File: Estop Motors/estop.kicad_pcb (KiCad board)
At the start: 2 copper layers, 28 parts, among them Q1 IRF9530N, Q2 IRF9530N, Q3 IRF9530N, Q4 IRF9530N

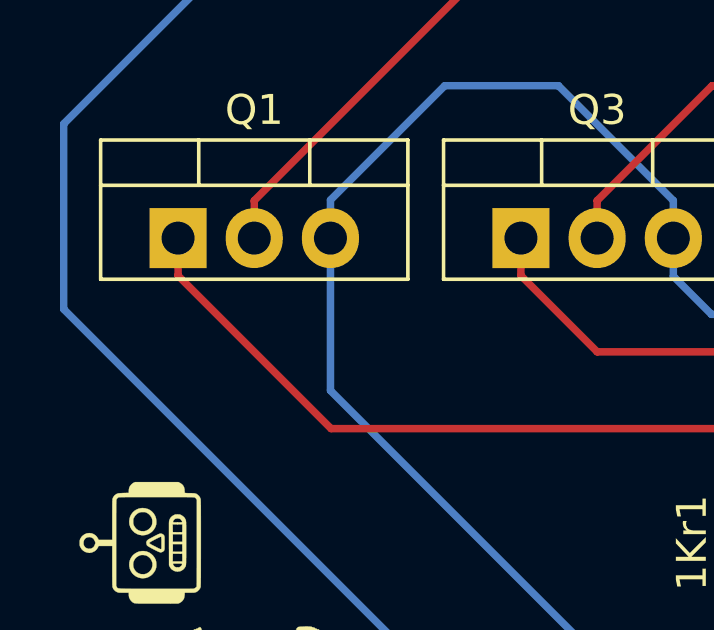
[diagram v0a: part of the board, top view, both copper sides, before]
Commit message: Fixed Silkscreen
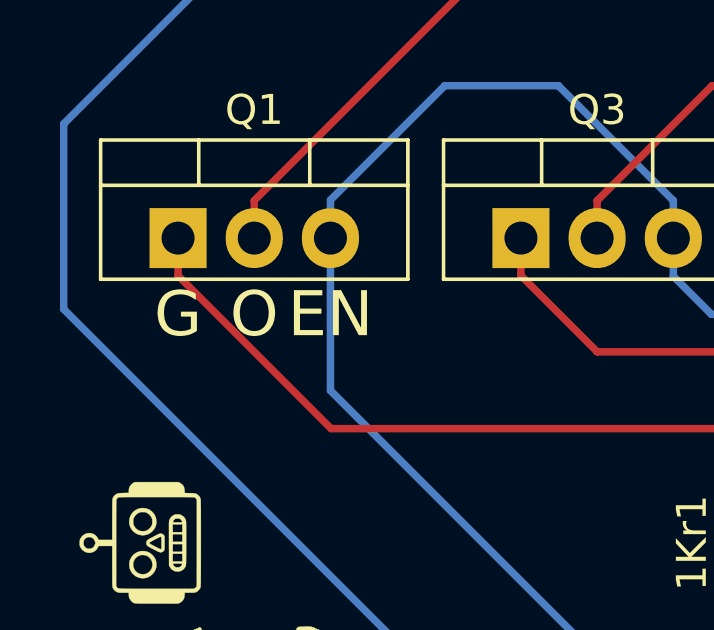
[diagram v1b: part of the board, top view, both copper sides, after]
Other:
- board text added: "EN"
- board text added: "G"
- board text added: "O"
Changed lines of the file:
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@@
   (general
     (thickness 1.6)
-    (drawings 1)
+    (drawings 4)
     (tracks 79)
     (zones 0)
@@
       (outputformat 1)
       (mirror false)
-      (drillshape 1)
+      (drillshape 0)
       (scaleselection 1)
-      (outputdirectory "./"))
+      (outputdirectory "../../GIB/Estop/"))
   )
   (net 0 "")
@@
     )
   )
+  (gr_text EN (at 77.47 127) (layer F.SilkS)
+    (effects (font (size 1.5 1.5) (thickness 0.3)))
+  )
+  (gr_text O (at 74.93 127) (layer F.SilkS)
+    (effects (font (size 1.5 1.5) (thickness 0.3)))
+  )
+  (gr_text "G\n" (at 72.39 127) (layer F.SilkS)
+    (effects (font (size 1.5 1.5) (thickness 0.3)))
+  )
   (gr_text "Motor Controller Override\nRev3" (at 118.11 135.89 90) (layer F.SilkS)
